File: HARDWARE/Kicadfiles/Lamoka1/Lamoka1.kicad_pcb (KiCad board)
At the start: 2 copper layers, 155.4 x 124.8 mm, 109 parts, among them IC1 INA240A2DR, J1 2606-1108/010-000, J2 2606-1352, J3 USB_C_Receptacle_USB2.0_14P, J4 470531000, J5 2604-1103, J6 Male-Header, J7 Male-Header, Q1 25V 60A N-Ch, Q2 30V 56A N-Ch, Q3 100V 150A N-Ch, Q4 100V 150A N-Ch, Q5 100V 150A N-Ch, Q6 100V 150A N-Ch, SW1 B3F-4055, U1 RP2354A, U10 ADS7128IRTER, U2 AMS1117-3.3, U3 74AHCT1G125, U4 LM5122MH/NOPB, U5 UCC27735DR, U6 UCC27735DR, U7 TPS62160DSGR, U8 TMP235A2DBZR, U9 TMP235A2DBZR

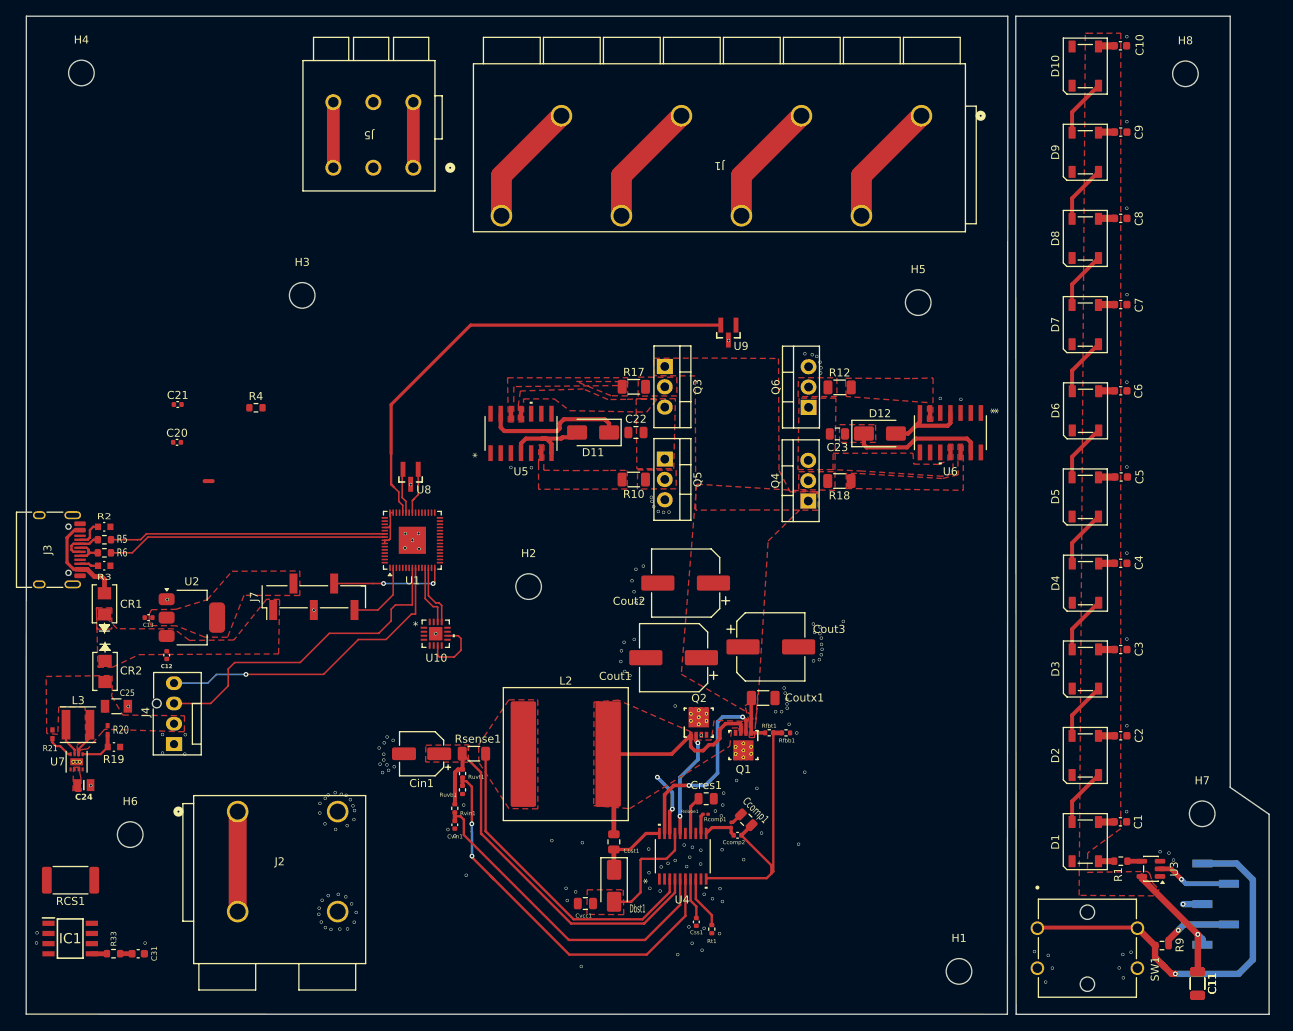
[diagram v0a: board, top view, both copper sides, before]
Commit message: More various routing, finish assigning of all components in inversion and control section. ADD interactive BOM, clean up documentation
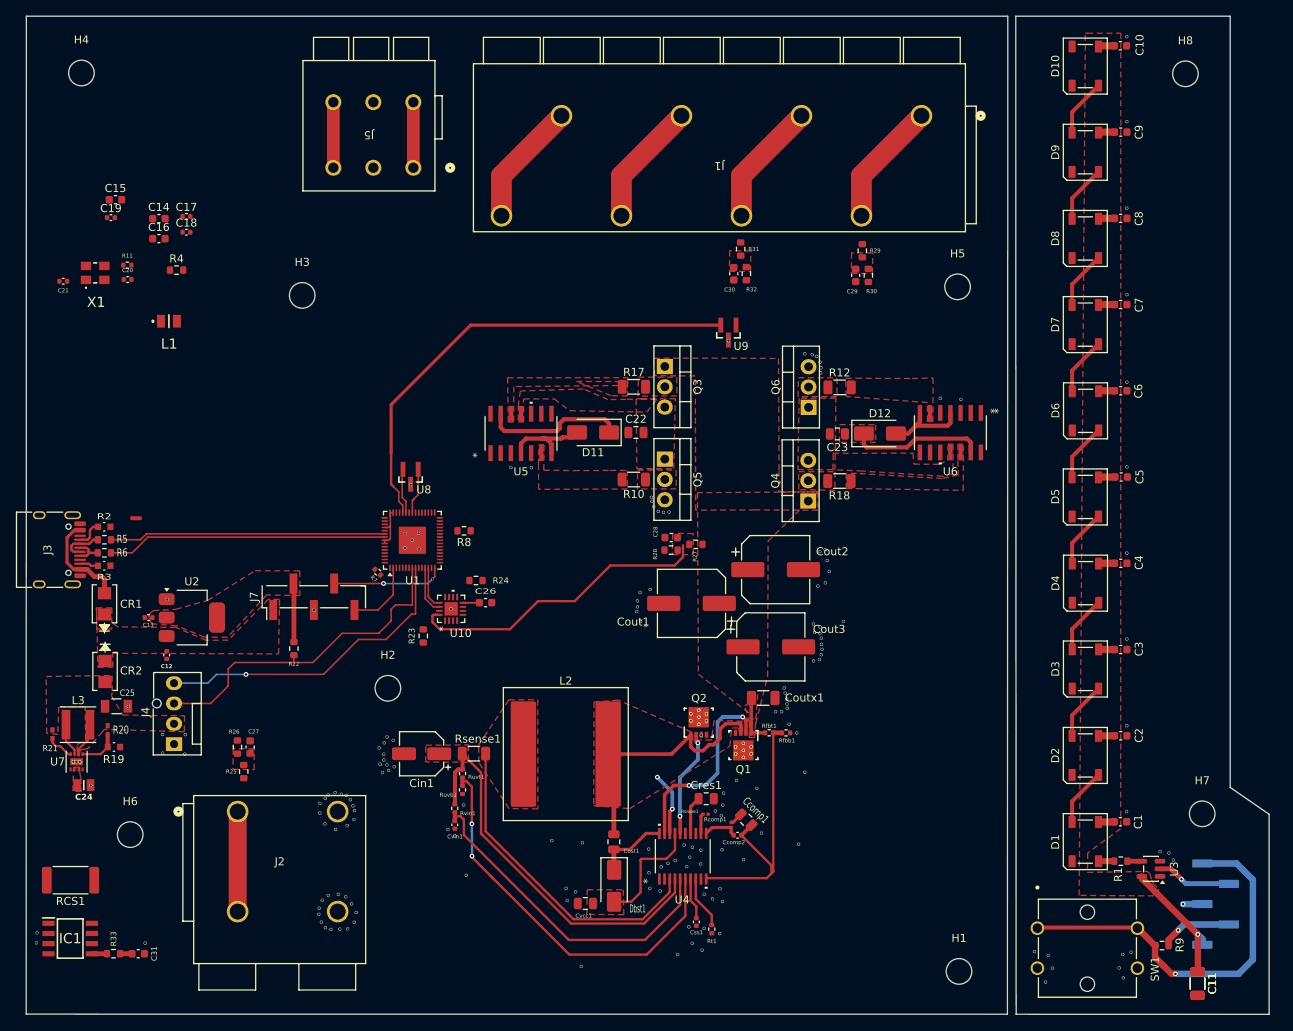
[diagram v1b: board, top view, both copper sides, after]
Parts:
- added C14: 4.7u, Capacitor_SMD:C_0603_1608Metric, F.Cu at (72.4, 54.9)
- added C15: 4.7u, Capacitor_SMD:C_0603_1608Metric, F.Cu at (67.0, 52.5)
- added C16: 4.7u, Capacitor_SMD:C_0603_1608Metric, F.Cu at (72.4, 57.4)
- added C17: 100n, Capacitor_SMD:C_0402_1005Metric, F.Cu at (75.8, 54.6)
- added C18: 100n, Capacitor_SMD:C_0402_1005Metric, F.Cu at (75.8, 56.6)
- added C19: 100n, Capacitor_SMD:C_0402_1005Metric, F.Cu at (66.4, 54.8)
- added C26: 1uF, Capacitor_SMD:C_0603_1608Metric, F.Cu at (113.2, 102.9)
- added C27: 47nF, Capacitor_SMD:C_0603_1608Metric, F.Cu at (83.8, 121.0)
- added C28: 47nF, Capacitor_SMD:C_0603_1608Metric, F.Cu at (136.4, 94.8)
- added C29: 47nF, Capacitor_SMD:C_0603_1608Metric, F.Cu at (159.5, 62.0)
- added C30: 47nF, Capacitor_SMD:C_0603_1608Metric, F.Cu at (144.2, 61.8)
- added L1: 3.3u, AOTA-B201610S3R3-101-T:AOTAB201610S3R3101T, F.Cu at (73.6, 67.7)
- added R11: 1k, Resistor_SMD:R_0402_1005Metric, F.Cu at (68.4, 60.7)
- added R22: 10k, Resistor_SMD:R_0603_1608Metric, F.Cu at (89.3, 108.7)
- added R23: 4.7k, Resistor_SMD:R_0603_1608Metric, F.Cu at (105.4, 107.1)
- added R24: 4.7k, Resistor_SMD:R_0603_1608Metric, F.Cu at (112.0, 100.1)
- added R25: 36.5k, Resistor_SMD:R_0603_1608Metric, F.Cu at (83.0, 124.0)
- added R26: 10k, Resistor_SMD:R_0603_1608Metric, F.Cu at (82.2, 121.0)
- added R27: 43.2k, Resistor_SMD:R_0603_1608Metric, F.Cu at (139.5, 95.6)
- added R28: 10k, Resistor_SMD:R_0603_1608Metric, F.Cu at (136.4, 96.3)
- added R29: 45.3k, Resistor_SMD:R_0603_1608Metric, F.Cu at (160.3, 58.9)
- added R30: 10k, Resistor_SMD:R_0603_1608Metric, F.Cu at (161.1, 62.0)
- added R31: 45.3k, Resistor_SMD:R_0603_1608Metric, F.Cu at (145.1, 58.7)
- added R32: 10k, Resistor_SMD:R_0603_1608Metric, F.Cu at (145.8, 61.8)
- added R7: 1k, Resistor_SMD:R_0402_1005Metric, F.Cu at (99.7, 99.1)
- added R8: 10k, Resistor_SMD:R_0603_1608Metric, F.Cu at (110.5, 93.9)
- added X1: ABM8-272-T3, ABM8-272-T3:ABM8272T3, F.Cu at (64.4, 61.7)
- moved H2 21.7 mm to (101.0, 113.6)
- moved C20 21.3 mm to (68.5, 62.5)
- moved C21 21.0 mm to (60.4, 62.7), turned to 180 degrees
- moved R4 19.9 mm to (74.6, 61.3)
- moved Cout2 11.4 mm to (149.5, 98.8), turned to 0 degrees
- moved NT1 10.2 mm to (69.5, 92.3), turned to 180 degrees
- moved Cout1 7.14 mm to (139.0, 103.0)
- moved H5 5.30 mm to (172.2, 63.4)
- moved U10 3.66 mm to (108.9, 103.7), turned to 90 degrees
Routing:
- net /Control-Section/AIN1: track 0.00 -> 38.6 mm
- net /Control-Section/GPIO9: track 7.70 -> 5.30 mm
- net Net-(U10-DECAP): track 0.00 -> 2.07 mm
- net /Control-Section/GPIO8: track 7.71 -> 6.31 mm
- net /GPIO5: track 41.6 -> 42.5 mm
- net /Control-Section/3v3: track 19.5 -> 18.9 mm
- added copper zone on F.Cu, net /Control-Section/AIN0
- added copper zone on F.Cu, net /Control-Section/AIN1
- added copper zone on F.Cu, net /Control-Section/AIN2
- added copper zone on F.Cu, net /Control-Section/AIN3

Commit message: Route 1v1 converter for control section of Lamoka1
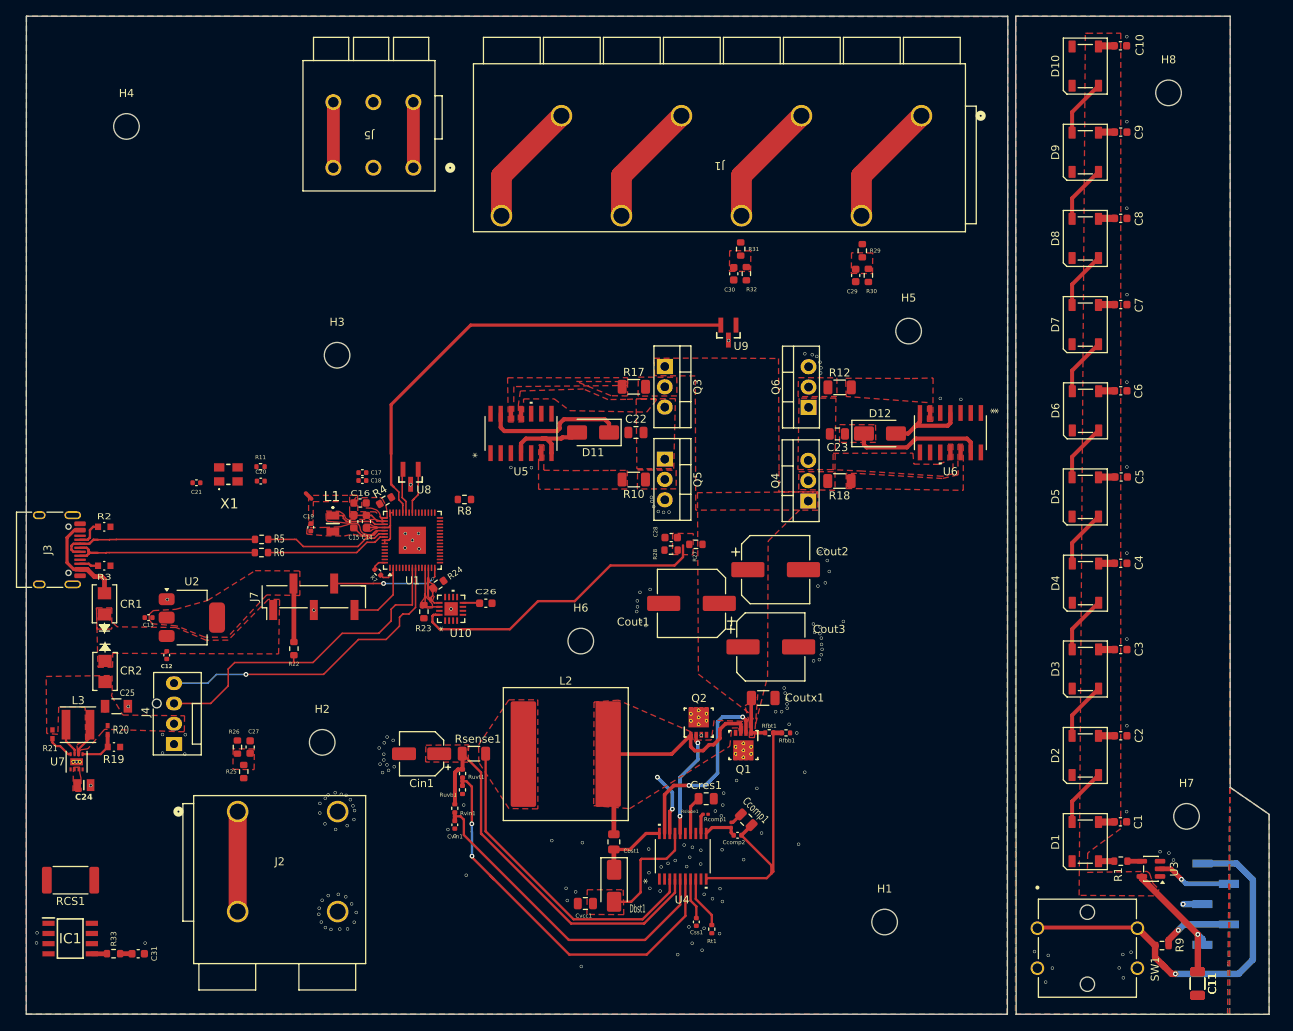
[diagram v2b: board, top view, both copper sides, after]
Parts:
- moved H6 61.3 mm to (125.1, 107.7)
- moved C15 50.1 mm to (96.8, 92.8), turned to 90 degrees
- moved C19 46.1 mm to (91.4, 93.5), turned to 90 degrees
- moved C14 45.9 mm to (98.3, 92.8), turned to 90 degrees
- moved C16 41.5 mm to (97.5, 90.5), turned to 180 degrees
- moved R4 38.9 mm to (100.7, 90.2), turned to -150 degrees
- moved C17 38.8 mm to (97.8, 86.7), turned to 180 degrees
- moved C18 38.0 mm to (97.8, 87.6), turned to 180 degrees
- moved L1 32.5 mm to (94.1, 93.0), turned to -90 degrees
- moved C21 30.2 mm to (77.1, 87.9)
- moved R11 30.2 mm to (85.1, 85.9)
- moved C20 30.2 mm to (85.1, 87.7)
- moved X1 30.2 mm to (81.1, 86.9)
- moved NT1 21.7 mm to (91.1, 89.6), turned to 135 degrees
- moved R5 19.7 mm to (85.2, 95.0)
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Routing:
- net /Control-Section/D-: track 5.29 -> 25.0 mm
- net /Control-Section/USB_DP: track 35.0 -> 15.4 mm
- net /Control-Section/D+: track 4.07 -> 23.7 mm
- net /Control-Section/USB_DM: track 34.5 -> 15.6 mm
- net Net-(U1-VREG_LX): track 0.00 -> 7.08 mm
- net /Control-Section/1V1: track 0.00 -> 4.51 mm
- net /Control-Section/VREG_GND: track 0.00 -> 4.17 mm
- net /Control-Section/3v3: track 18.9 -> 21.2 mm
- net /Control-Section/BTN: track 8.98 -> 10.9 mm
- net Net-(U1-~{QSPI_SS}): track 0.00 -> 1.79 mm
- net /Control-Section/GPIO9: track 5.30 -> 6.82 mm
- net /Control-Section/GPIO8: track 6.31 -> 6.87 mm
- added copper zone on F.Cu, net /Control-Section/1V1
- added copper zone on F.Cu, net /Control-Section/GPIO8
- added copper zone on F.Cu, net /Control-Section/GPIO9
- added copper zone on F.Cu, net /Control-Section/VREG_GND
- added copper zone on B.Cu, net GND
- added copper zone on F.Cu, net GND
- added copper zone on F.Cu, net Net-(U1-VREG_AVDD)
- added copper zone on F.Cu, net Net-(U1-VREG_LX)

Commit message: Route in crystall oscillator for control section. Fix a ton of DRC issues, etc
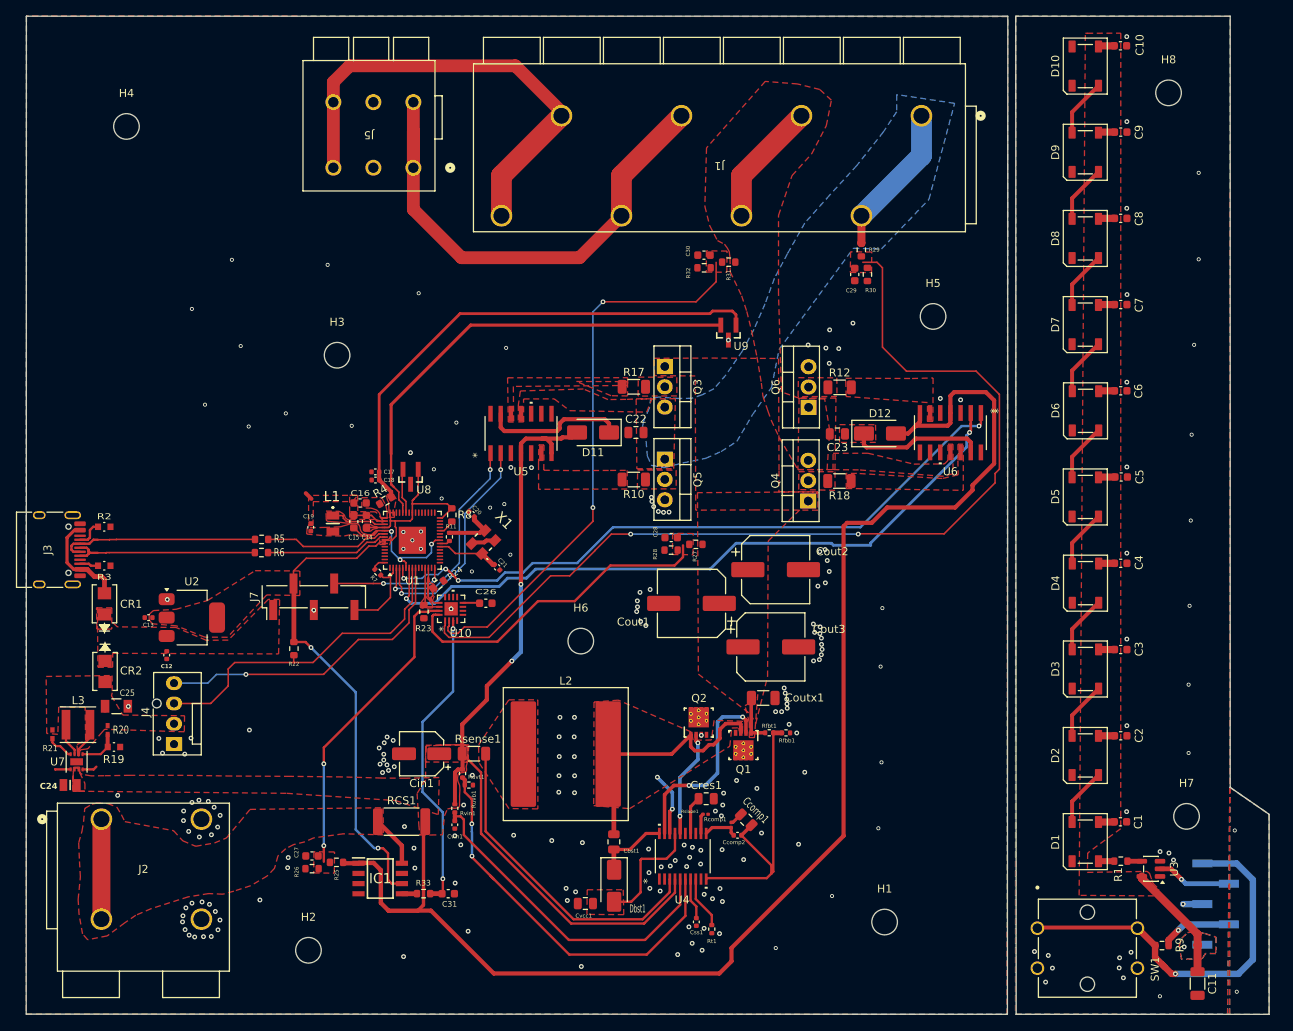
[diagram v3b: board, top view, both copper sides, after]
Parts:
- removed the C11 at (202.2, 150.5)
- moved RCS1 42.0 mm to (102.7, 130.3), turned to 0 degrees
- moved C31 39.5 mm to (108.6, 139.3)
- moved IC1 39.5 mm to (100.0, 137.4)
- moved R33 39.5 mm to (105.5, 139.3)
- moved C21 39.0 mm to (114.7, 98.5), turned to -45 degrees
- moved X1 33.0 mm to (113.0, 95.3), turned to 45 degrees
- moved C20 26.7 mm to (111.5, 91.8), turned to 135 degrees
- moved H2 26.0 mm to (91.1, 146.4)
- moved R11 25.2 mm to (108.7, 94.7), turned to -90 degrees
- moved R26 17.8 mm to (91.5, 136.2), turned to 180 degrees
- moved J2 17.1 mm to (65.2, 130.0)
- moved R25 16.2 mm to (94.6, 135.4), turned to 180 degrees
- moved C27 15.7 mm to (91.5, 134.6), turned to 180 degrees
- moved R32 5.34 mm to (140.5, 61.0), turned to 180 degrees
- moved C30 4.39 mm to (140.5, 59.5), turned to 180 degrees
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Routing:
- net /Inversion-Section/CSP: track 73.6 -> 281.1 mm, vias 0 -> 2
- net /Control-Section/3v3: track 21.2 -> 149.6 mm, vias 0 -> 2
- net /Control-Section/AIN2: track 0.00 -> 119.7 mm, vias 0 -> 2
- net /Control-Section/GPIO4: track 0.00 -> 87.2 mm, vias 0 -> 2
- net /Control-Section/GPIO3: track 0.00 -> 84.1 mm, vias 0 -> 4
- net /Control-Section/AIN3: track 0.00 -> 70.9 mm, vias 0 -> 2
- net /BLACK: track 23.8 -> 64.3 mm
- net /Control-Section/AIN0: track 0.00 -> 38.8 mm, vias 0 -> 2
- net /Control-Section/AIN4: track 1.48 -> 38.3 mm, vias 0 -> 2
- net /RED: track 23.8 -> 58.5 mm
- net /Control-Section/GPIO2: track 0.00 -> 28.4 mm, vias 0 -> 2
- net /Control-Section/GPIO1: track 0.00 -> 27.4 mm, vias 0 -> 2
- net /Control-Section/1V1: track 4.51 -> 17.6 mm, vias 0 -> 3
- net /Control-Section/5V: track 10.2 -> 0.11 mm
- net /User-Interface-Section/5V: track 26.4 -> 35.0 mm
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- added copper zone on B.Cu, net /BLUE
- added copper zone on F.Cu, net /Battery-Connection 
- added copper zone on B.Cu, net /User-Interface-Section/5V
- added copper zone on F.Cu, net /User-Interface-Section/5V

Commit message: Refine a few things, vias, doccumentation, etc
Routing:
- net GND: track 9.29 -> 24.6 mm, vias 222 -> 227
- net /Inversion-Section/HO: track 24.5 -> 23.7 mm

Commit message: General fixes to DRC, etc (Lamoka1/2)
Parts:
- added G***: LOGO, LOGO, F.Cu at (79.2, 58.3)
- moved H3 10.1 mm to (94.9, 82.1)
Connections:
- Q1 pad 9: (no net) -> GND
- Q2 pad 9: (no net) -> GND
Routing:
- net /Control-Section/3v3: track 149.6 -> 201.0 mm, vias 2 -> 5
- net /Control-Section/1V1: track 17.6 -> 24.7 mm
- net GND: track 24.6 -> 26.4 mm, vias 227 -> 240
- added copper zone on F.Cu, net /Inversion-Section/HB1
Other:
- board text added: "Lamoka1/2"
- board text added: "Rated for 100% internal magic smoke retention."

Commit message: misc fixes to Lamoka1/2
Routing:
- net /BLACK: track 64.3 -> 68.2 mm
- net /RED: track 58.5 -> 62.3 mm
- net /Inversion-Section/UVLO: track 49.5 -> 46.7 mm
- net /Inversion-Section/CSP: track 281.1 -> 278.9 mm
- net /Inversion-Section/VIN: track 42.0 -> 40.4 mm
- net /Control-Section/3v3: track 201.0 -> 201.6 mm
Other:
- board text added: "3V3"
- board text added: "5V"
- board text added: "BLACK"
- board text added: "BLUE"
- board text added: "BROWN"
- board text added: "BTN"
- board text added: "GND"
- board text added: "GPIO11"
- board text added: "GRAY"
- board text added: "ORANGE"
- board text added: "RED"
- board text added: "VIOLET"
- board text added: "YELLOW"

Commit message: Get DRC down all the way, other misc improvements
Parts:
- moved C29 3.68 mm to (159.4, 65.6)
- moved R30 3.68 mm to (161.0, 65.6)
- moved R29 3.68 mm to (160.3, 62.5)
- moved C30 3.40 mm to (137.1, 59.8)
- moved R32 3.40 mm to (137.1, 61.3)
- moved R31 3.40 mm to (140.2, 60.6)
- moved C1 1.00 mm to (193.6, 130.3)
- moved C10 1.00 mm to (193.6, 33.3)
- moved C11 1.00 mm to (203.2, 150.5)
- moved C2 1.00 mm to (193.6, 119.5)
- moved C3 1.00 mm to (193.6, 108.8)
- moved C4 1.00 mm to (193.6, 98.0)
- moved C5 1.00 mm to (193.7, 87.2)
- moved C6 1.00 mm to (193.6, 76.4)
- moved C7 1.00 mm to (193.6, 65.6)
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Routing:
- net /BROWN: track 15.6 -> 25.2 mm
- net /Control-Section/AIN2: track 119.7 -> 115.5 mm
- net /Control-Section/3v3: track 201.6 -> 197.6 mm
- net /BLUE: track 19.0 -> 22.7 mm
- net /Control-Section/AIN3: track 70.9 -> 67.7 mm
- net GND: track 26.4 -> 29.3 mm
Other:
- board size 155.4 x 124.8 mm -> 156.4 x 124.8 mm
